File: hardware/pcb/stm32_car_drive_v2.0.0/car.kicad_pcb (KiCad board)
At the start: 2 copper layers, 99.5 x 88.2 mm, 93 parts, among them J0 OLED, J1 DC母座(大), J10 Conn_01x03, J11 Conn_01x03, J12 Conn_01x03, J13 Conn_01x02, J14 OLED, J15 Conn_01x02, J17 Conn_01x05, J18 Conn_01x02, J19 Conn_01x02, J2 Conn_01x06, J20 Conn_01x09, J22 Conn_01x10, J23 Conn_01x04, J24 Conn_01x02, J25 HC-05, J26 Conn_01x08, J3 HC-05, J4 Conn_01x06, J5 Conn_01x03, J6 Conn_01x03, J7 Conn_01x03, J8 Conn_01x03, J9 Conn_01x03, K210 Conn_01x04, P1 USB_C_Plug_USB2.0, Q1 S8050, SW1 K1, SW2 K2, SW3 K3, SW4 K6, SW5 K5, SW6 K4, SW7 RST, SW8 SW_Push_SPDT, U1 STM32F103RCTx, U10 CH340C, U11 SGM2212-3.3XKC3G/TR, U5 DRV8870DDA, U7 TPS5430DDA, U8 DRV8870DDA, Y1 Crystal_GND24(8M)

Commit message: update
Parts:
- removed D6, D7: LED, Library:LED_0805_2012Metric
- removed D8: B340, Library:D_SMA
- removed HC-SR04: HC-SR04, Library:PinSocket_1x04_P2.54mm_Vertical
- removed J0: OLED, Library:PinSocket_1x04_P2.54mm_Vertical
- removed J24: Conn_01x02, Library:PinSocket_1x02_P2.54mm_Vertical
- removed J25: HC-05, Library:PinSocket_1x06_P2.54mm_Vertical
- removed J26: Conn_01x08, Library:PinHeader_1x06_P2.54mm_Vertical
- removed R10, R11: 10k, Library:R_0603_1608Metric
- removed SW4: K6, Library:SW_Push_1P1T_NO_6x6mm
- removed SW5: K5, Library:SW_Push_1P1T_NO_6x6mm
- added D1: B340, Diode_SMD:D_SMA, F.Cu at (224.1, 106.7)
- added J16: HC-05, Connector_PinSocket_2.54mm:PinSocket_1x06_P2.54mm_Vertical, F.Cu at (-34.1, 221.0)
- added J21: Conn_01x03, Connector_PinHeader_2.54mm:PinHeader_1x03_P2.54mm_Vertical, F.Cu at (234.1, 82.8)
- added L2: 22uh, DuRuofu_L:L_Wuerth_HCI-1040, F.Cu at (204.3, 108.3)
- added OLED1: OLED_0.96, DuRuofu_Module:0.96OLED_4P, F.Cu at (86.5, 54.5)
- added R3: 0, Resistor_SMD:R_0603_1608Metric, F.Cu at (185.0, 66.5)
- added R4: 0, Resistor_SMD:R_0603_1608Metric, F.Cu at (185.1, 69.6)
- BZ2: footprint Library:Indicator_PUI_AI-1440-TWT-24V-2-R -> Buzzer_Beeper:Indicator_PUI_AI-1440-TWT-24V-2-R
- C1, C2, C23, C5: footprint Library:CP_Elec_6.3x7.7 -> Capacitor_SMD:CP_Elec_6.3x7.7
- C10, C11, C12, C13, C14, C15, C16, C17, C18, C19, C20, C21, C22, C3, C4, C6, C9: footprint Library:C_0603_1608Metric -> Capacitor_SMD:C_0603_1608Metric
- D2, D3, D4, D5: footprint Library:LED_0805_2012Metric -> LED_SMD:LED_0805_2012Metric
- J1: footprint Library:DC母座(大) -> DuRuofu_Connector:DC母座(大)
- J10, J12, J5, J6: value Conn_01x03 -> Conn_01x02; footprint Library:PinSocket_1x03_P2.54mm_Vertical -> Connector_PinHeader_2.54mm:PinHeader_1x02_P2.54mm_Vertical
- J11, J7, J8, J9: footprint Library:PinSocket_1x03_P2.54mm_Vertical -> Connector_PinSocket_2.54mm:PinSocket_1x03_P2.54mm_Vertical
- J13: footprint Library:CONN-TH_2P-P5.08 -> DuRuofu_Connector:CONN-TH_2P-P5.08
- J14: value OLED -> Conn_01x03; footprint Library:PinSocket_1x04_P2.54mm_Vertical -> Connector_PinHeader_2.54mm:PinHeader_1x03_P2.54mm_Vertical
- J15: value Conn_01x02 -> Conn_01x03; footprint Library:HDR-TH_2P-P2.00-V-F-1 -> Connector_PinHeader_2.54mm:PinHeader_1x03_P2.54mm_Vertical
- J17: value Conn_01x05 -> Conn_01x03; footprint Library:PinSocket_1x05_P2.54mm_Vertical -> Connector_PinHeader_2.54mm:PinHeader_1x03_P2.54mm_Vertical
- J18: footprint Library:PinSocket_1x02_P2.54mm_Vertical -> Connector_PinHeader_2.54mm:PinHeader_1x02_P2.54mm_Vertical
- J19: value Conn_01x02 -> Conn_01x08; footprint Library:PinSocket_1x02_P2.54mm_Vertical -> DuRuofu_Module:MPU6050-GY-521
- J2, J4: footprint Library:JST_XH_S6B-XH-A_1x06_P2.50mm_Horizontal -> Connector_JST:JST_XH_S6B-XH-A_1x06_P2.50mm_Horizontal
- J20: value Conn_01x09 -> Conn_02x08_Counter_Clockwise; footprint Library:PinSocket_1x09_P2.54mm_Vertical -> Connector_PinHeader_2.54mm:PinHeader_2x08_P2.54mm_Vertical
- J22: footprint Library:JST_XH_B8B-XH-A_1x08_P2.50mm_Vertical -> Connector_JST:JST_XH_B8B-XH-A_1x08_P2.50mm_Vertical
- J23: footprint Library:PinSocket_1x04_P2.54mm_Vertical -> Connector_PinSocket_2.54mm:PinSocket_1x04_P2.54mm_Vertical
- J3: footprint Library:PinSocket_1x06_P2.54mm_Vertical -> Connector_PinSocket_2.54mm:PinSocket_1x06_P2.54mm_Vertical
- K210: footprint Library:JST_XH_B4B-XH-A_1x04_P2.50mm_Vertical -> Connector_JST:JST_XH_B4B-XH-A_1x04_P2.50mm_Vertical
- P1: footprint Library:USB_C_Receptacle_GCT_USB4105-xx-A_16P_TopMnt_Horizontal -> Connector_USB:USB_C_Receptacle_GCT_USB4105-xx-A_16P_TopMnt_Horizontal
- Q1: footprint Library:SOT-23 -> Package_TO_SOT_SMD:SOT-23
- R1, R2: footprint Library:R_1206_3216Metric -> Resistor_SMD:R_1206_3216Metric
- R12, R13, R14, R15, R18, R5, R6, R7, R8, R9: footprint Library:R_0603_1608Metric -> Resistor_SMD:R_0603_1608Metric
- R16, R17: footprint Library:R_0805_2012Metric -> Resistor_SMD:R_0603_1608Metric
- SW1, SW2, SW3, SW6: footprint Library:SW_Push_1P1T_NO_6x6mm -> DuRuofu_Switch:SW_Push_1P1T_NO_6x6mm
- SW7: footprint Library:SW_SPST_FSMSM -> Button_Switch_SMD:SW_SPST_FSMSM
- SW8: footprint Library:SW_CuK_JS202011CQN_DPDT_Straight -> Button_Switch_THT:SW_CuK_JS202011CQN_DPDT_Straight
- U1: footprint Library:LQFP-64_10x10mm_P0.5mm -> Package_QFP:LQFP-64_10x10mm_P0.5mm
- U10: footprint Library:SOIC-16_3.9x9.9mm_P1.27mm -> Package_SO:SOIC-16_3.9x9.9mm_P1.27mm
- U11: footprint Library:SOT-223 -> Package_TO_SOT_SMD:SOT-223
- U2, U3, U4, U6: footprint Library:SOT-363_SC-70-6 -> Package_TO_SOT_SMD:SOT-363_SC-70-6
- U5, U8: footprint Library:Texas_HTSOP-8-1EP_3.9x4.9mm_P1.27mm_EP2.95x4.9mm_Mask2.4x3.1mm_ThermalVias -> Package_SO:Texas_HTSOP-8-1EP_3.9x4.9mm_P1.27mm_EP2.95x4.9mm_Mask2.4x3.1mm_ThermalVias
- U7: footprint Library:TI_SO-PowerPAD-8_ThermalVias -> Package_SO:TI_SO-PowerPAD-8_ThermalVias
- Y1: footprint Library:Crystal_SMD_3225-4Pin_3.2x2.5mm -> Crystal:Crystal_SMD_3225-4Pin_3.2x2.5mm
- moved SW8 281.3 mm to (219.7, 122.2)
- moved BZ2 267.9 mm to (211.9, 93.9)
- moved R18 266.6 mm to (215.5, 119.0)
- moved R14 263.8 mm to (212.2, 119.0)
- moved D5 255.5 mm to (211.4, 51.6)
- moved C23 255.1 mm to (204.4, 119.8), turned to -90 degrees
- moved U11 250.3 mm to (193.1, 99.1), turned to 90 degrees
- moved C19 244.9 mm to (207.9, 64.8), turned to 90 degrees
- moved C20 244.3 mm to (207.9, 76.5), turned to -90 degrees
- moved SW6 236.9 mm to (182.6, 119.8)
- moved C22 233.1 mm to (196.5, 78.5), turned to 180 degrees
- moved C21 232.3 mm to (195.7, 76.2), turned to -90 degrees
- moved R16 232.2 mm to (200.4, 87.9)
- moved Y1 232.0 mm to (200.4, 85.0)
- moved R17 225.5 mm to (193.0, 72.8), turned to 90 degrees
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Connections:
- net /PA10 renamed /KEY1
- net /PB12 renamed /Buzzer
- net /PB6 renamed /USART1_TX
- net /PB7 renamed /USART1_RX
- D3 pad 1: /PA8 -> /LED1
- D4 pad 1: /PB3 -> /LED2
- D5 pad 1: /PD2 -> /LED3
- J10 pad 1: +3.3V -> /USART4_TX
- J10 pad 2: +3.3V -> /USART4_RX
- J12 pad 1: +5V -> /USART5_TX
- J12 pad 2: +5V -> /USART5_RX
- J14 pad 1: GND -> /TIM3_CH1
- J14 pad 2: +3.3V -> +5V
- J14 pad 3: /PB8 -> GND
- J15 pad 1: /PC8 -> /TIM3_CH2
- J15 pad 2: /PC9 -> +5V
- J17 pad 1: /PA4 -> /TIM3_CH3
- J17 pad 2: /PA5 -> +5V
- J17 pad 3: /PA6 -> GND
- J19 pad 1: /PB10 -> +3.3V
- J19 pad 2: /PB11 -> GND
- J2 pad 3: /PB4 -> /TIM1_CH2
- J2 pad 4: /PB5 -> /TIM1_CH1
- J20 pad 1: GND -> /-PB2
- J20 pad 2: /PB4 -> /-PB3
- J20 pad 3: /PB5 -> /-PC0
- J20 pad 4: /PC10 -> /-PC1
- J20 pad 5: /PC11 -> /-PC2
- J20 pad 6: /PC4 -> /-PC3
- J20 pad 7: /PA15 -> /-PC4
- J20 pad 8: /PC6 -> /-PC5
- J20 pad 9: /PC7 -> /-PC8
- J3 pad 4: /PB10 -> /USART3_TX
- J3 pad 5: /PB11 -> /USART3_RX
- J4 pad 3: /PA0 -> /TIM8_CH2
- J4 pad 4: /PA1 -> /TIM8_CH1
- J5 pad 1: GND -> /USART2_TX
- J5 pad 2: GND -> /USART2_RX
- J6 pad 1: GND -> /USART3_TX
- J6 pad 2: GND -> /USART3_RX
- K210 pad 1: /PA2 -> /USART2_TX
- K210 pad 2: /PA3 -> /USART2_RX
- SW2 pad 1: /PA11 -> /KEY2
- SW3 pad 1: /PA12 -> /KEY3
- SW6 pad 1: /PB15 -> /KEY4
- U1 pad 10: /PC2 -> /-PC2
- U1 pad 11: /PC3 -> /-PC3
- U1 pad 14: /PA0 -> /TIM2_CH1
- U1 pad 15: /PA1 -> /TIM2_CH2
- U1 pad 16: /PA2 -> /USART2_TX
- U1 pad 17: /PA3 -> /USART2_RX
- U1 pad 2: /PC13 -> /-PC13
- U1 pad 20: /PA4 -> /DIRA
- U1 pad 21: /PA5 -> /DIRB
- U1 pad 22: /PA6 -> /TIM3_CH1
- U1 pad 23: /PA7 -> /TIM3_CH2
- U1 pad 24: /PC4 -> /-PC4
- U1 pad 25: /PC5 -> /-PC5
- U1 pad 26: /PB0 -> /TIM3_CH3
- U1 pad 27: /PB1 -> /TIM3_CH4
- U1 pad 28: /PB2 -> /-PB2
- U1 pad 29: /PB10 -> /USART3_TX
- U1 pad 3: /PC14 -> /-PC14
- U1 pad 30: /PB11 -> /USART3_RX
- U1 pad 34: /PB13 -> /LED1
- U1 pad 35: /PB14 -> /LED2
- U1 pad 36: /PB15 -> /LED3
- U1 pad 37: /PC6 -> /TIM8_CH1
- U1 pad 38: /PC7 -> /TIM8_CH2
- U1 pad 39: /PC8 -> /-PC8
- U1 pad 4: /PC15 -> /-PC15
- U1 pad 40: /PC9 -> /-PC9
- U1 pad 41: /PA8 -> /TIM1_CH1
- U1 pad 42: /PA9 -> /TIM1_CH2
- U1 pad 44: /PA11 -> /KEY2
- U1 pad 45: /PA12 -> /KEY3
- U1 pad 50: /PA15 -> /KEY4
- U1 pad 51: /PC10 -> /USART4_TX
- U1 pad 52: /PC11 -> /USART4_RX
- U1 pad 53: /PC12 -> /USART5_TX
- U1 pad 54: /PD2 -> /USART5_RX
- U1 pad 55: /PB3 -> /-PB3
- U1 pad 56: /PB4 -> /MPU_SCL
- U1 pad 57: /PB5 -> /MPU_SDA
- U1 pad 61: /PB8 -> /OLED_SDA
- U1 pad 62: /PB9 -> /OLED_ACL
- U1 pad 8: /PC0 -> /-PC0
- U1 pad 9: /PC1 -> /-PC1
- U10 pad 2: /PA11 -> Net-(U10-TXD)
- U10 pad 3: /PA12 -> Net-(U10-RXD)
- U2 pad 1: /PA8 -> /TIM2_CH1
- U2 pad 6: /PC14 -> /DIRA
- U3 pad 3: /PA9 -> /TIM2_CH2
- U3 pad 6: /PC15 -> /DIRB
- U4 pad 1: /PA9 -> /TIM2_CH2
- U4 pad 6: /PC15 -> /DIRB
- U6 pad 3: /PA8 -> /TIM2_CH1
- U6 pad 6: /PC14 -> /DIRA
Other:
- board size 99.5 x 88.2 mm -> 101.3 x 106.8 mm

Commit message: feat(pcb): 更新PCB封装
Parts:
- removed J22: Conn_01x10, Connector_JST:JST_XH_B8B-XH-A_1x08_P2.50mm_Vertical
- added J24: Conn_01x04, Connector_PinSocket_2.54mm:PinSocket_1x04_P2.54mm_Vertical, F.Cu at (106.4, 141.0)
- J19: footprint DuRuofu_Module:MPU6050-GY-521 -> Library:MPU6050-GY-521
- OLED1: footprint DuRuofu_Module:0.96OLED_4P -> Library:0.96OLED_4P
- P1: footprint Connector_USB:USB_C_Receptacle_GCT_USB4105-xx-A_16P_TopMnt_Horizontal -> Library:USB_C_Receptacle_GCT_USB4105-xx-A_16P_TopMnt_Horizontal
- SW1, SW2, SW3, SW6: footprint DuRuofu_Switch:SW_Push_1P1T_NO_6x6mm -> Library:SW_Push_1P1T_NO_6x6mm
- U10: footprint Package_SO:SOIC-16_3.9x9.9mm_P1.27mm -> Library:SOIC-16_3.9x9.9mm_P1.27mm
- moved J16 161.7 mm to (80.2, 106.5)
- moved J3 145.3 mm to (96.8, 109.1)
- moved J9 145.3 mm to (105.3, 128.4)
- moved J11 111.8 mm to (81.7, 139.6)
- moved J7 111.8 mm to (77.7, 139.6)
- moved OLED1 88.2 mm to (172.0, 76.0)
- moved J8 70.3 mm to (85.3, 131.9)
- moved K210 45.6 mm to (90.5, 119.2)
- moved SW1 43.1 mm to (134.7, 133.1)
- moved U7 43.1 mm to (180.2, 134.8)
- moved C1 43.1 mm to (195.6, 66.9)
- moved C2 43.1 mm to (141.2, 66.4)
- moved C23 43.1 mm to (167.8, 142.5)
- moved J14 43.1 mm to (197.4, 109.8)
- moved J15 43.1 mm to (197.3, 114.2)
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
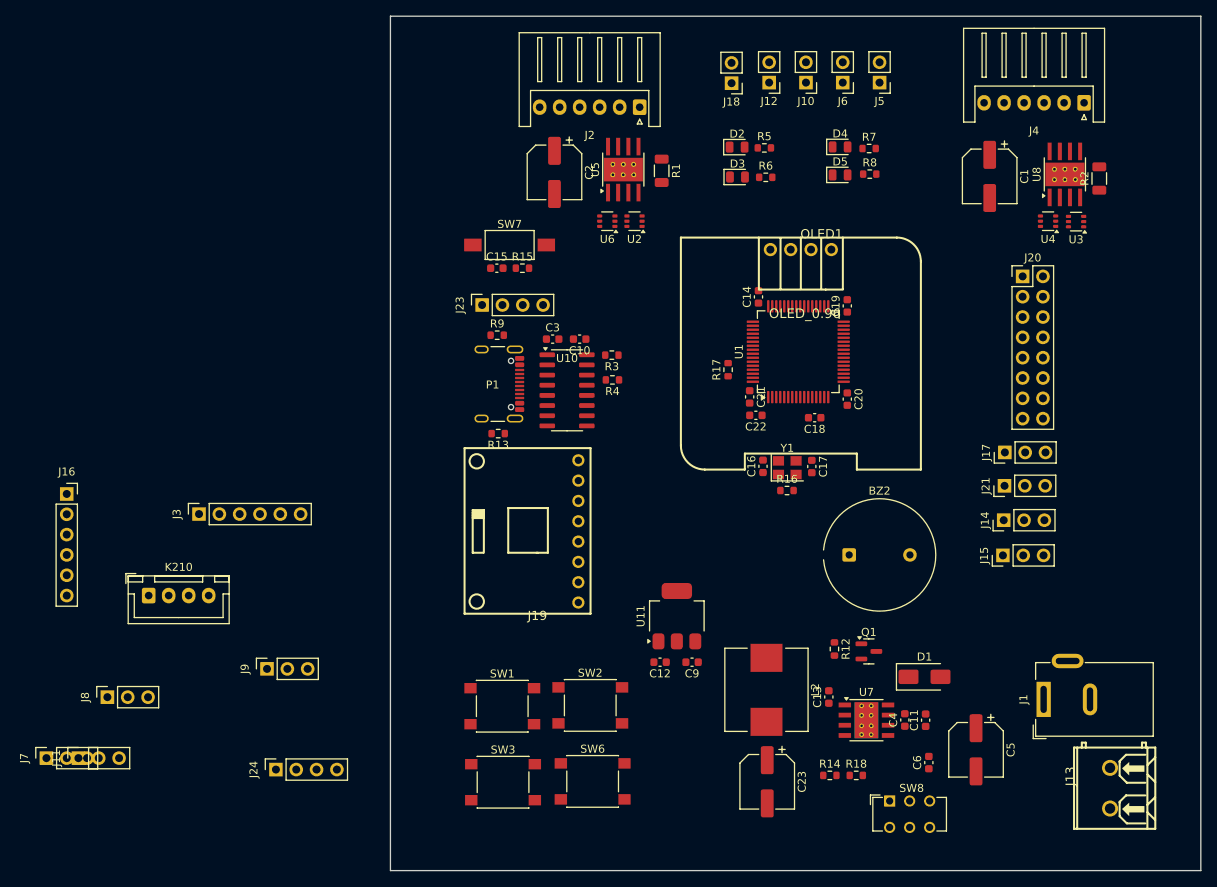
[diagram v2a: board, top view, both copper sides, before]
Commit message: feat(pcb):更新布局
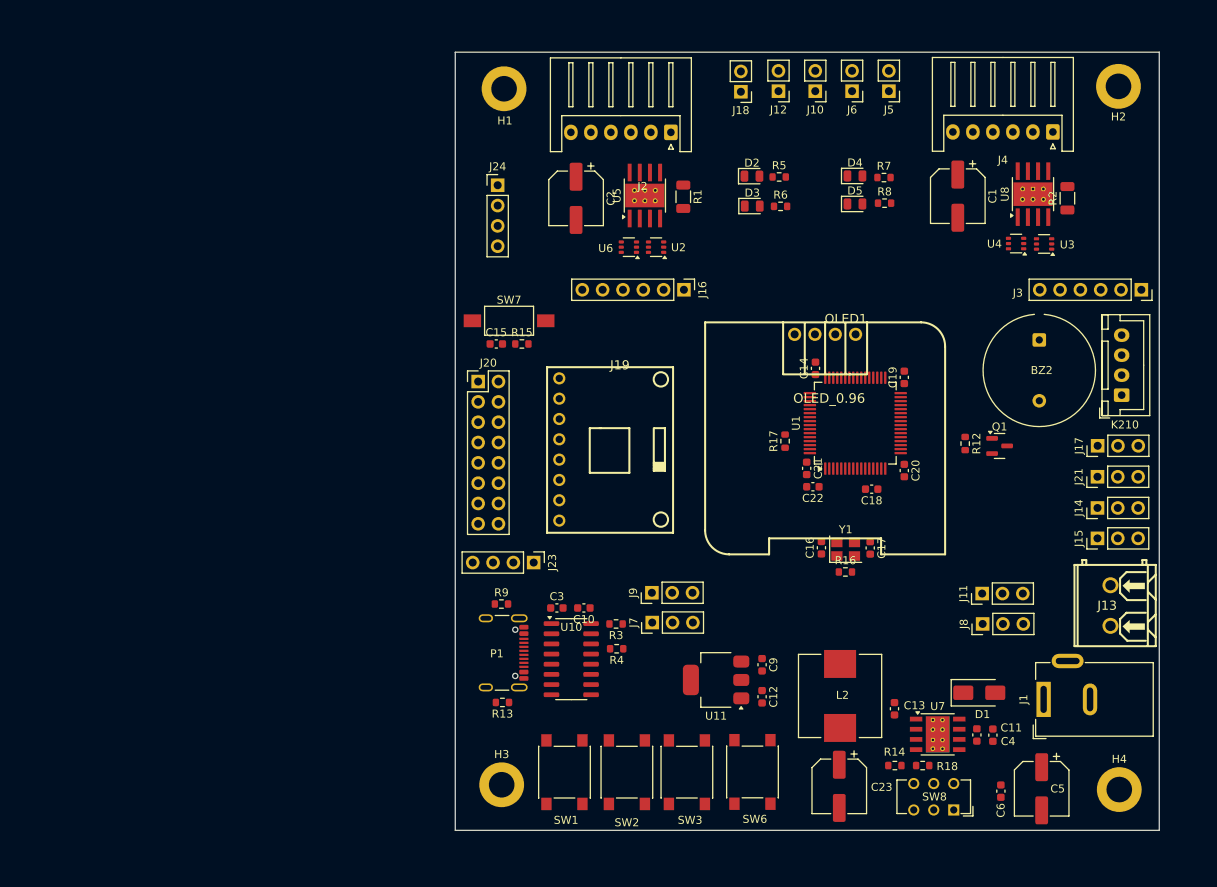
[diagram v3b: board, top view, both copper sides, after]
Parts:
- added H1: MountingHole, MountingHole:MountingHole_3.2mm_M3_DIN965_Pad, F.Cu at (134.9, 55.9)
- added H2: MountingHole, MountingHole:MountingHole_3.2mm_M3_DIN965_Pad, F.Cu at (211.7, 55.6)
- added H3: MountingHole, MountingHole:MountingHole_3.2mm_M3_DIN965_Pad, F.Cu at (134.6, 142.9)
- added H4: MountingHole, MountingHole:MountingHole_3.2mm_M3_DIN965_Pad, F.Cu at (211.8, 143.5)
- J11, J7, J8, J9: footprint Connector_PinSocket_2.54mm:PinSocket_1x03_P2.54mm_Vertical -> Connector_PinHeader_2.54mm:PinHeader_1x03_P2.54mm_Vertical
- J16: footprint Connector_PinSocket_2.54mm:PinSocket_1x06_P2.54mm_Vertical -> Connector_PinHeader_2.54mm:PinHeader_1x06_P2.54mm_Vertical
- J23, J24: footprint Connector_PinSocket_2.54mm:PinSocket_1x04_P2.54mm_Vertical -> Connector_PinHeader_2.54mm:PinHeader_1x04_P2.54mm_Vertical
- moved K210 124.2 mm to (212.1, 94.2), turned to 90 degrees
- moved J3 121.1 mm to (214.6, 81.0), turned to -90 degrees
- moved J11 114.8 mm to (194.7, 119.0)
- moved J8 109.8 mm to (194.7, 122.8)
- moved J16 81.3 mm to (157.4, 81.0), turned to -90 degrees
- moved J24 78.1 mm to (134.1, 68.0), turned to 0 degrees
- moved J7 77.6 mm to (153.4, 122.6)
- moved J20 69.3 mm to (131.7, 92.5)
- moved J9 49.0 mm to (153.4, 118.9)
- moved BZ2 35.9 mm to (201.8, 87.3), turned to -90 degrees
- moved R13 33.6 mm to (134.7, 132.6)
- moved C10 33.6 mm to (144.9, 120.8)
- moved C3 33.6 mm to (141.5, 120.8)
- moved R3 33.6 mm to (148.9, 122.8)
- moved R4 33.6 mm to (149.0, 125.9)
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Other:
- board size 101.3 x 106.8 mm -> 88 x 97.3 mm

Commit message: 连线
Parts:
- DIO CLK 3.3 GND: renamed from J23
- PB2 PB3: renamed from J20
- moved SW7 0.55 mm to (135.9, 84.5)
- moved C9 0.32 mm to (167.2, 128.2)
- renumbered J9 to 3.3V, J11 to 5V, J14 to CH1, J15 to CH2, J21 to CH4, J17 to CH5, J24 to EIGHT-WAY, J8 to GND, J7 to GND, SW1 to KEY1, SW2 to KEY2, SW3 to KEY3, SW6 to KEY4, J19 to MPU6050, J18 to UART1, J5 to UART2, J6 to UART3, J10 to UART4, J12 to UART5, SW8 to 电源
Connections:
- KEY1 pad 2: +3V3 -> +3.3V
- KEY2 pad 2: +3V3 -> +3.3V
- KEY3 pad 2: +3V3 -> +3.3V
- KEY4 pad 2: +3V3 -> +3.3V
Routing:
- net GND: track 0.00 -> 514.0 mm, vias 0 -> 53
- net +3.3V: track 0.00 -> 423.7 mm, vias 0 -> 26
- net +12V: track 0.00 -> 178.9 mm, vias 0 -> 7
- net +5V: track 0.00 -> 163.4 mm, vias 0 -> 4
- net /USART1_RX: track 0.00 -> 103.6 mm, vias 0 -> 5
- net /USART2_RX: track 0.00 -> 101.3 mm, vias 0 -> 1
- net /USART2_TX: track 0.00 -> 100.2 mm, vias 0 -> 1
- net /-PB2: track 0.00 -> 94.4 mm, vias 0 -> 7
- net /USART1_TX: track 0.00 -> 93.4 mm, vias 0 -> 4
- net /USART3_RX: track 0.00 -> 81.8 mm, vias 0 -> 1
- net /USART3_TX: track 0.00 -> 80.8 mm, vias 0 -> 1
- net /KEY1: track 0.00 -> 77.7 mm, vias 0 -> 4
- net /USART4_RX: track 0.00 -> 74.1 mm, vias 0 -> 5
- net /KEY2: track 0.00 -> 73.3 mm, vias 0 -> 4
- net /KEY3: track 0.00 -> 71.9 mm, vias 0 -> 4
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- added copper zone on F.Cu, net +12V
- added copper zone on F.Cu, net +3.3V
- added copper zone on F.Cu, net +5V
- added copper zone on B.Cu, net GND
- added copper zone on F.Cu, net GND
- added copper zone on F.Cu, net Net-(BZ2-+)
- added copper zone on F.Cu, net Net-(D1-K)
- added copper zone on F.Cu, net Net-(U7-VSENSE)
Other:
- board text added: "5V"
- board text added: "5V GND"
- board text added: "HC-05"
- board text added: "PB2 PB3 PC0 PC1 PC2 PC3 PC4 PC5 PC8 PC9 PC13 PC14 PC15 GND GND 3.3"
- board text added: "RX"
- board text added: "RX TX"
- board text added: "TOF25"

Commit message: feat: 生成生产文件
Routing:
- net GND: track 514.0 -> 516.6 mm, vias 53 -> 54
- net Net-(D1-K): track 1.09 -> 3.50 mm, vias 1 -> 0
- net +12V: track 178.9 -> 180.9 mm
- removed copper zone on F.Cu, net Net-(BZ2-+)
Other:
- outline, holes or cut-outs redrawn
- board text added: "@duruofu @yangbin 2024/6/21"
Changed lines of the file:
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@@
 		)
 	)
-	(gr_rect
-		(start 128.8 51.33)
-		(end 216.8 148.6)
+	(gr_line
+		(start 128.8 145.6)
+		(end 128.8 54.33)
+		(stroke
+			(width 0.05)
+			(type default)
+		)
+		(layer "Edge.Cuts")
+	)
+	(gr_arc
+		(start 213.8 51.33)
+		(mid 215.92132 52.20868)
+		(end 216.8 54.33)
+		(stroke
+			(width 0.05)
+			(type default)
+		)
+		(layer "Edge.Cuts")
+	)
+	(gr_line
+		(start 213.8 148.6)
+		(end 131.8 148.6)
+		(stroke
+			(width 0.05)
+			(type default)
+		)
+		(layer "Edge.Cuts")
+	)
+	(gr_arc
+		(start 131.8 148.6)
+		(mid 129.67868 147.72132)
+		(end 128.8 145.6)
+		(stroke
+			(width 0.05)
+			(type default)
+		)
+		(layer "Edge.Cuts")
+	)
+	(gr_line
+		(start 216.8 54.33)
+		(end 216.8 145.6)
+		(stroke
+			(width 0.05)
+			(type default)
+		)
+		(layer "Edge.Cuts")
+	)
+	(gr_line
+		(start 131.8 51.33)
+		(end 213.8 51.33)
+		(stroke
+			(width 0.05)
+			(type default)
+		)
+		(layer "Edge.Cuts")
+	)
+	(gr_arc
+		(start 216.8 145.6)
+		(mid 215.92132 147.72132)
+		(end 213.8 148.6)
+		(stroke
+			(width 0.05)
+			(type default)
+		)
+		(layer "Edge.Cuts")
+	)
+	(gr_arc
+		(start 128.8 54.33)
+		(mid 129.67868 52.20868)
+		(end 131.8 51.33)
 		(stroke
 			(width 0.05)
 			(type default)
 		)
-		(fill none)
 		(layer "Edge.Cuts")
 	)
@@
 		)
 	)
+	(gr_text "@duruofu\n@yangbin\n2024/6/21"
+		(at 168.91 80.01 0)
+		(layer "F.SilkS")
+		(effects
+			(font
+				(size 1.5 1.5)
+				(thickness 0.3)
+				(bold yes)
+			)
+			(justify left bottom)
+		)
+	)
 	(gr_text "5V"
 		(at 132.3 68.6 90)
@@
 	)
 	(segment
+		(start 136.8 122)
+		(end 138.6 120.2)
+		(width 0.6)
+		(layer "F.Cu")
+		(net 1)
+	)
+	(segment
 		(start 149.295 118.5)
 		(end 143.025 118.5)
@@
 	)
 	(segment
+		(start 136.8 122.09)
+		(end 136.8 122)
+		(width 0.6)
+		(layer "F.Cu")
+		(net 1)
+	)
+	(segment
 		(start 188.05 140.5)
 		(end 189.7 140.5)
@@
 	)
 	(via
+		(at 135 121.4)
+		(size 0.6)
+		(drill 0.3)
+		(layers "F.Cu" "B.Cu")
+		(free yes)
+		(net 1)
+	)
+	(via
 		(at 204.2 69.8)
 		(size 0.6)
@@
 	)
 	(segment
+		(start 194.025 135.925)
+		(end 194 135.9)
+		(width 0.35)
+		(layer "F.Cu")
+		(net 2)
+	)
+	(segment
 		(start 191.615 66.625)
 		(end 195.44 62.8)
@@
 		(net 2)
 	)
+	(segment
+		(start 196 135.925)
+		(end 194.025 135.925)
+		(width 0.35)
+		(layer "F.Cu")
+		(net 2)
+	)
 	(via
 		(at 188.3 64.6)
@@
 		(net 15)
 	)
-	(via
-		(at 191.8 133.6)
-		(size 0.6)
-		(drill 0.3)
-		(layers "F.Cu" "B.Cu")
+	(segment
+		(start 191.8 133.6)
+		(end 192.3 133.1)
+		(width 0.2)
+		(layer "F.Cu")
 		(net 15)
 	)
 	(segment
-		(start 185.88 134.175)
-		(end 186.4 134.695)
+		(start 192.3 133.1)
+		(end 192.3 131.4)
 		(width 0.2)
 		(layer "F.Cu")
+		(net 15)
+	)
+	(segment
+		(start 186.4 134.695)
+		(end 184.22 134.695)
+		(width 0.35)
+		(layer "F.Cu")
 		(net 16)
 	)
 	(segment
-		(start 183.7 134.175)
-		(end 185.88 134.175)
-		(width 0.2)
+		(start 184.22 134.695)
+		(end 183.7 134.175)
+		(width 0.35)
 		(layer "F.Cu")
 		(net 16)
@@
 	)
 	(segment
-		(start 190.5575 148)
-		(end 200.395 148)
-		(width 0.2)
+		(start 202.345 132.23)
+		(end 202.345 146.905)
+		(width 0.8)
 		(layer "B.Cu")
 		(net 51)
 	)
 	(segment
-		(start 188.6075 146.05)
-		(end 190.5575 148)
-		(width 0.2)
+		(start 201.75 147.5)
+		(end 190.0575 147.5)
+		(width 0.8)
 		(layer "B.Cu")
 		(net 51)
 	)
 	(segment
-		(start 202.345 146.05)
-		(end 202.345 132.23)
-		(width 0.2)
+		(start 202.345 146.905)
+		(end 201.75 147.5)
+		(width 0.8)
 		(layer "B.Cu")
 		(net 51)
 	)
 	(segment
-		(start 200.395 148)
-		(end 202.345 146.05)
-		(width 0.2)
+		(start 190.0575 147.5)
+		(end 188.6075 146.05)
+		(width 0.8)
 		(layer "B.Cu")
 		(net 51)
@@
 			)
 		)
-	)
-	(zone
-		(net 6)
-		(net_name "Net-(BZ2-+)")
-		(layer "F.Cu")
-		(hatch edge 0.5)
-		(priority 11)
-		(connect_pads
-			(clearance 0.5)
-		)
-		(min_thickness 0.25)
-		(filled_areas_thickness no)
-		(fill yes
-			(thermal_gap 0.5)
-			(thermal_bridge_width 0.5)
-		)
-		(polygon
-			(pts
-				(xy 134.7 119.4) (xy 134.7 122.5) (xy 135.7 122.5) (xy 135.7 123.6) (xy 138.7 123.6) (xy 138.7 123.3)
-				(xy 142.1 123.3) (xy 142.2 122.1) (xy 141.4 122.1) (xy 141.4 119.4)
-			)
-		)
